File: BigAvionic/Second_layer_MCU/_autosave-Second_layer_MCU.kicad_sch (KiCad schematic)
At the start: 98 parts, among them J1 Conn_01x04, J10 Conn_01x04, J11 Conn_01x04, J13 Conn_01x08, J14 Conn_01x08, J2 USB_C_Receptacle_USB2.0_16P, J3 Conn_01x02, J4 Micro_SD_Card_Det1, J5 Conn_01x04, J6 Conn_01x04, J7 Screw_Terminal_01x02, J8 Conn_01x04, J9 Conn_01x08, Q2 BSS138, SW1 SW_Push, SW2 SW_Push_Shielded, SW3 SW_Push_Shielded, U1 STM32F405VGTx, U2 W25Q128JVS, U3 ADXL375BCCZ, U4 BMP390, U5 BMI088, Y1 FA-238 16Mhz

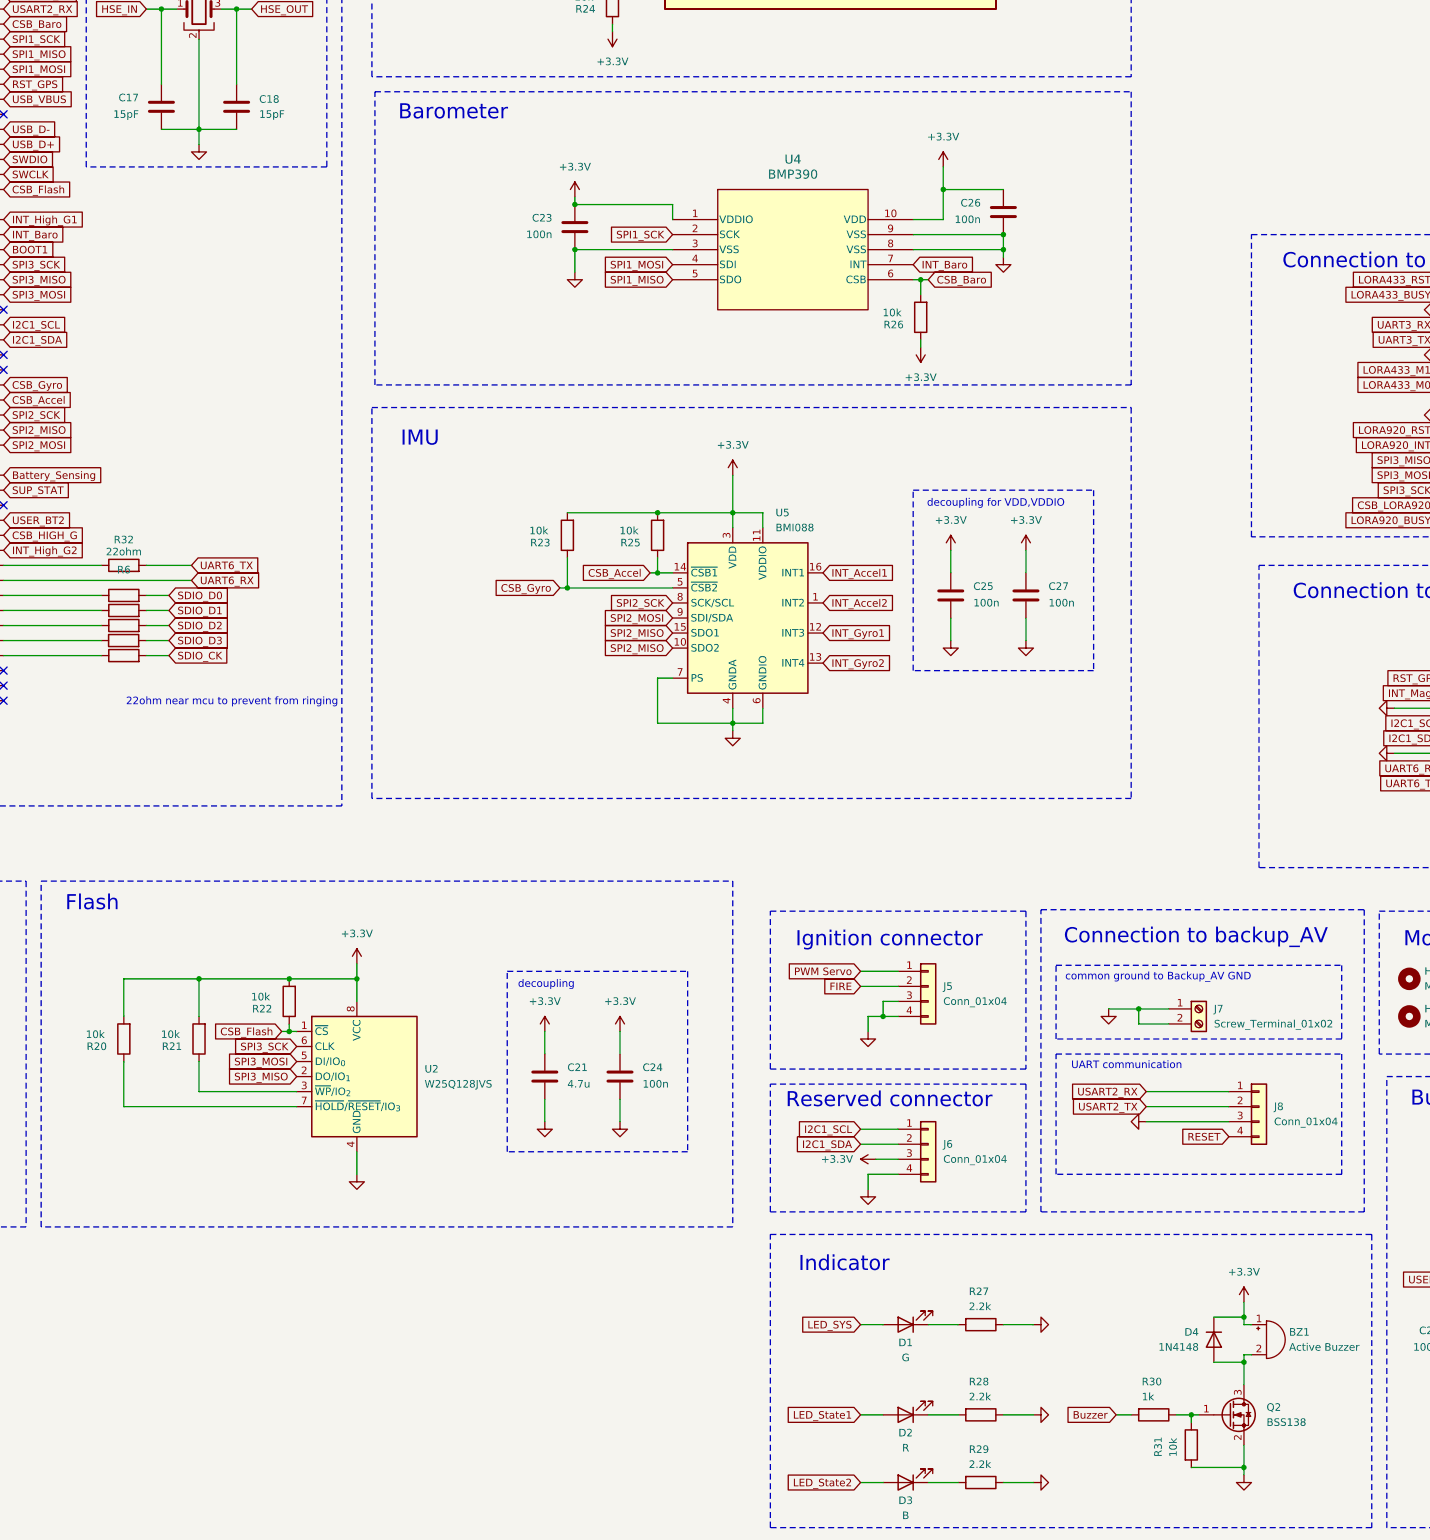
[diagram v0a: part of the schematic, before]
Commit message: edit some in MCU for production
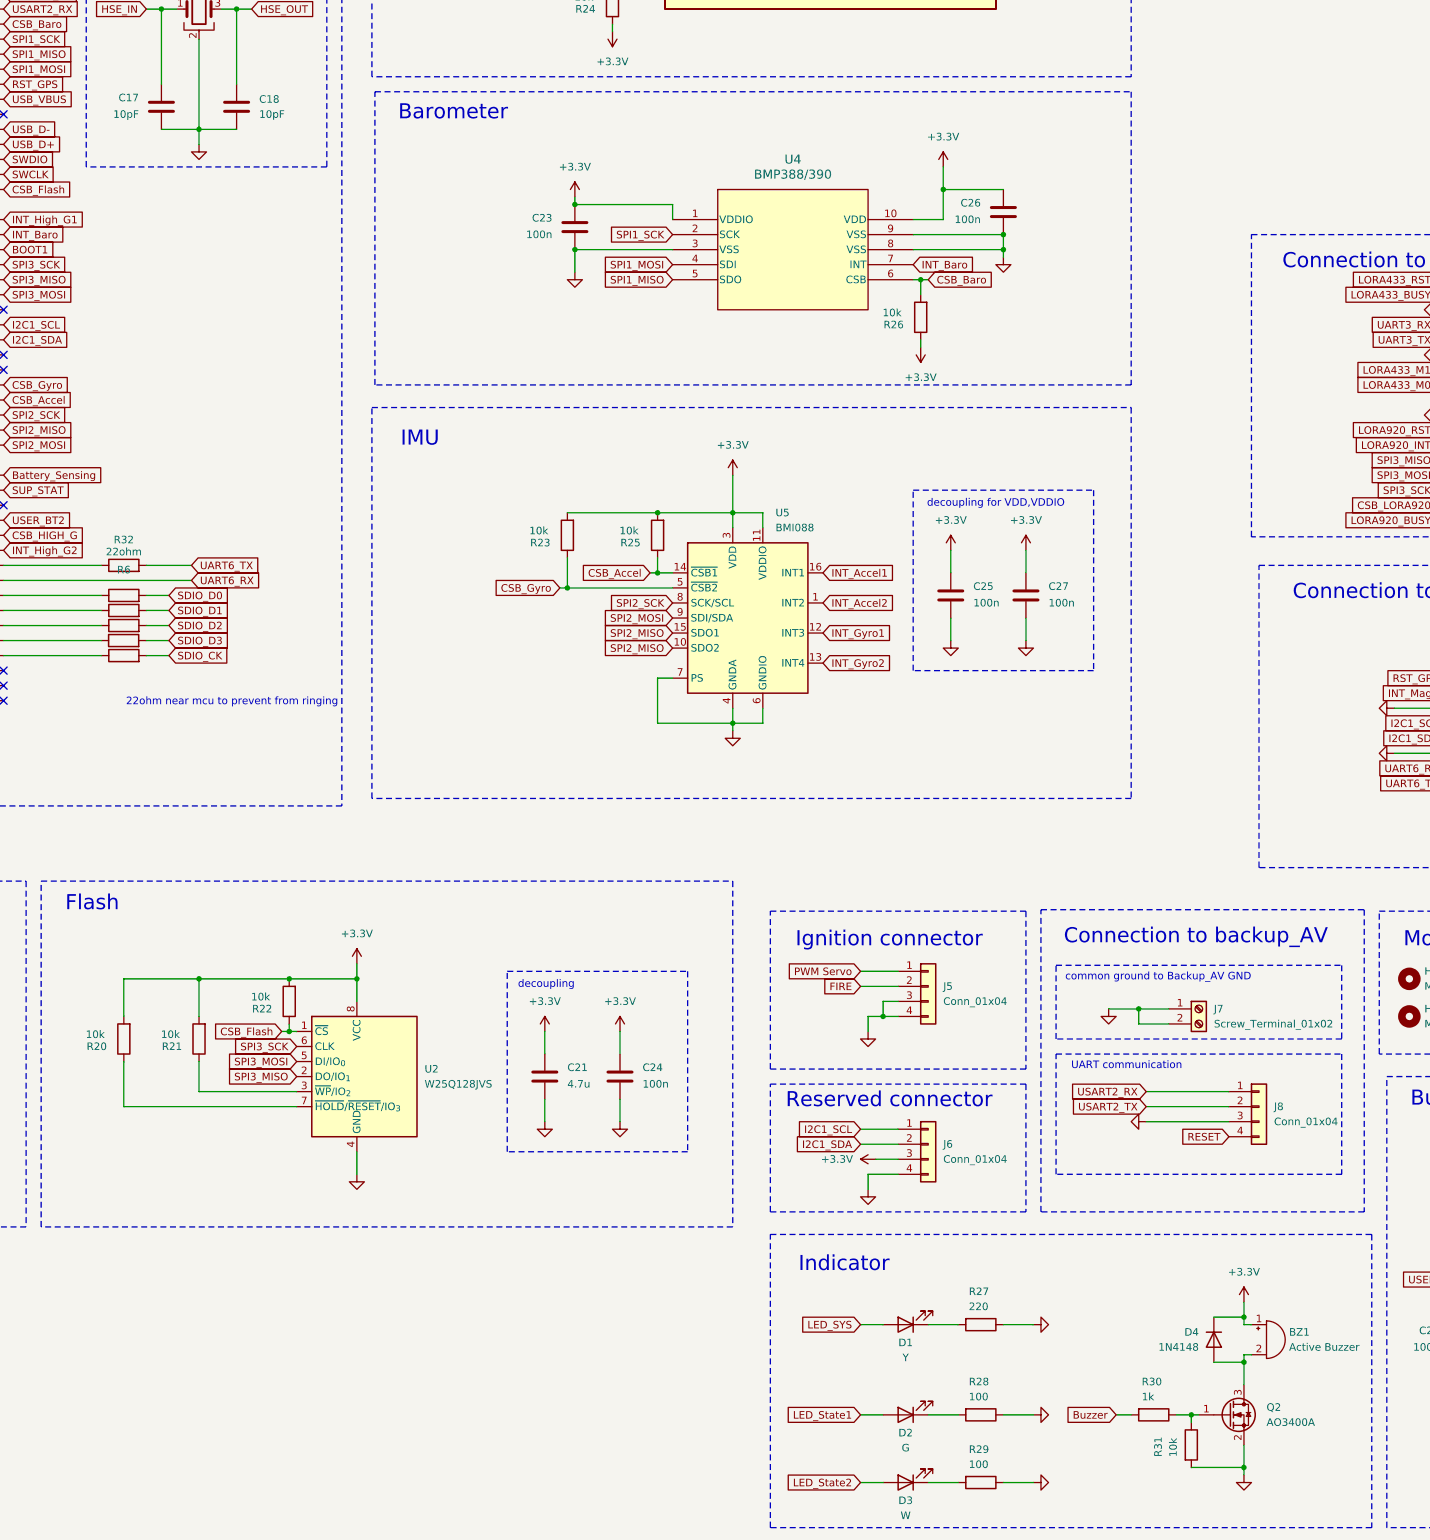
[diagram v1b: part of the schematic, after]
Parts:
- C17, C18: value 15pF -> 10pF
- D1: value G -> Y
- D2: value R -> G
- D3: value B -> W
- Q2: value BSS138 -> AO3400A
- R27: value 2.2k -> 220
- R28, R29: value 2.2k -> 100
- U4: value BMP390 -> BMP388/390
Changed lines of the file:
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@@
 			)
 		)
-		(property "Value" "BMP390"
+		(property "Value" "BMP388/390"
 			(at 284.48 107.95 0)
 			(effects
@@
 			)
 		)
-		(property "Value" "2.2k"
+		(property "Value" "220"
 			(at 314.198 299.212 90)
 			(effects
@@
 			)
 		)
-		(property "Value" "R"
+		(property "Value" "G"
 			(at 303.53 323.088 0)
 			(effects
@@
 			)
 		)
-		(property "Value" "2.2k"
+		(property "Value" "100"
 			(at 314.198 325.882 90)
 			(effects
@@
 			)
 		)
-		(property "Value" "BSS138"
+		(property "Value" "AO3400A"
 			(at 364.49 318.7699 0)
 			(effects
@@
 			)
 		)
-		(property "Value" "15pF"
+		(property "Value" "10pF"
 			(at 194.31 97.7899 0)
 			(effects
@@
 			)
 		)
-		(property "Value" "B"
+		(property "Value" "W"
 			(at 303.53 334.518 0)
 			(effects
@@
 			)
 		)
-		(property "Value" "2.2k"
+		(property "Value" "100"
 			(at 314.198 314.452 90)
 			(effects
@@
 			)
 		)
-		(property "Value" "G"
+		(property "Value" "Y"
 			(at 303.53 307.848 0)
 			(effects
@@
 			)
 		)
-		(property "Value" "15pF"
+		(property "Value" "10pF"
 			(at 173.99 97.7899 0)
 			(effects
